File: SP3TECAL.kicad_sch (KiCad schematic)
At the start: 15 parts, among them IC1 MM5230-03NDB-TR, IC2 MM5230-03NDB-TR, IC3 MM5230-03NDB-TR, IC4 MM5230-03NDB-TR, J1 Conn_Coaxial, J2 Conn_Coaxial, J3 Conn_Coaxial, J4 Conn_Coaxial, J5 Conn_01x04, J6 Conn_01x04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

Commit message: much progress on routing
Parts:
- added R4, R5, R6: 56k, Resistor_SMD:R_0402_1005Metric, symbol Device:R
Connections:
- net GND: now also R4.1, R5.1, R6.1
- net at IC1.2 (RF2), IC3.4 (RF4): now also R5.2
- net at IC1.1 (RF1), IC4.3 (RF3): now also R4.2
- net at IC1.3 (RF3), IC2.1 (RF1): now also R6.2

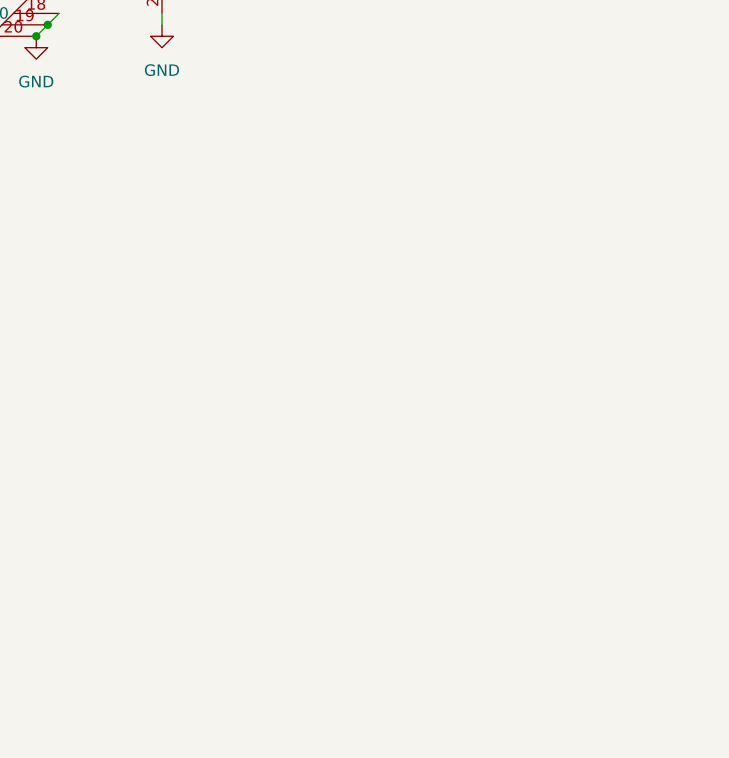
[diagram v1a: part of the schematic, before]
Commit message: used altium files to build kicad models of mm5800 and started new twpatron
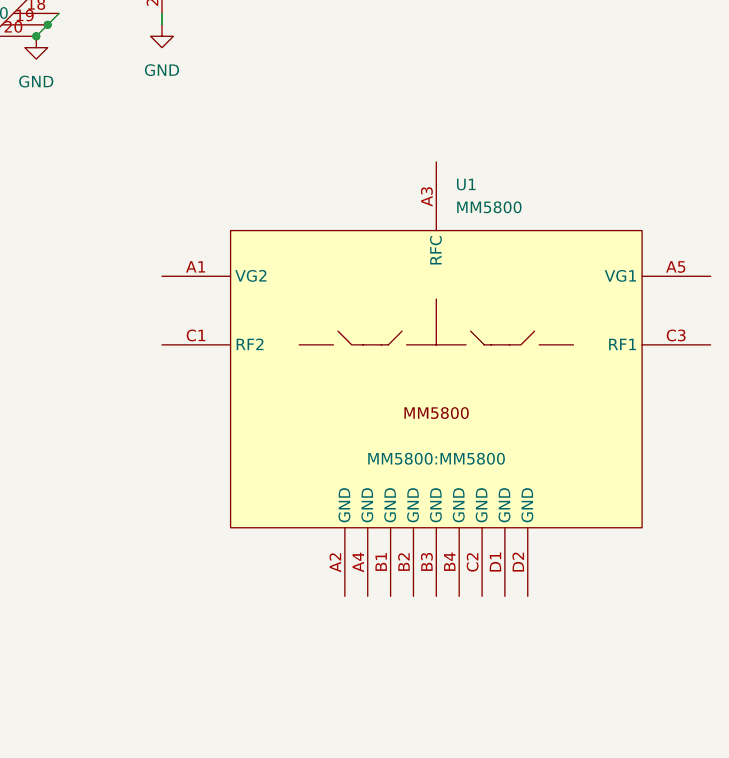
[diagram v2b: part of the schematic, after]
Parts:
- added U1: MM5800, MM5800:MM5800, symbol MM5800:MM5800.SCHLIB
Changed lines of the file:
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@@
+	)
+	(symbol
+		(lib_id "MM5800:MM5800.SCHLIB")
+		(at 245.11 123.19 0)
+		(unit 1)
+		(exclude_from_sim no)
+		(in_bom yes)
+		(on_board yes)
+		(dnp no)
+		(fields_autoplaced yes)
+		(property "Reference" "U1"
+			(at 247.2533 92.71 0)
+			(effects
+				(font
+					(size 1.27 1.27)
+				)
+				(justify left)
+			)
+		)
+		(property "Value" "MM5800"
+			(at 247.2533 95.25 0)
+			(effects
+				(font
+					(size 1.27 1.27)
+				)
+				(justify left)
+			)
+		)
+		(property "Footprint" "MM5800:MM5800"
+			(at 245.11 123.19 0)
+			(effects
+				(font
+					(size 1.27 1.27)
+				)
+			)
+		)
+		(property "Datasheet" ""
+			(at 245.11 123.19 0)
+			(effects
+				(font
+					(size 1.27 1.27)
+				)
+				(hide yes)
+			)
+		)
+		(property "Description" ""
+			(at 245.11 123.19 0)
+			(effects
+				(font
+					(size 1.27 1.27)
+				)
+				(hide yes)
+			)
+		)
+		(property "MANUFACTURER" "Menlo Micro"
+			(at 214.122 141.478 0)
+			(effects
+				(font
+					(size 1.27 1.27)
+				)
+				(justify left bottom)
+				(hide yes)
+			)
+		)
+		(property "MANUFACTURER_PART_NUMBER" "MM5800"
+			(at 214.122 141.478 0)
+			(effects
+				(font
+					(size 1.27 1.27)
+				)
+				(justify left bottom)
+				(hide yes)
+			)
+		)
+		(pin "A1"
+		)
+		(pin "C1"
+		)
+		(pin "B3"
+		)
+		(pin "A2"
+		)
+		(pin "B2"
+		)
+		(pin "D1"
+		)
+		(pin "B1"
+		)
+		(pin "A5"
+		)
+		(pin "A4"
+		)
+		(pin "C2"
+		)
+		(pin "A3"
+		)
+		(pin "C3"
+		)
+		(pin "B4"
+		)
+		(pin "D2"
+		)
+		(instances
+			(project ""
+				(path "/27633a03-897e-4d8a-8472-386b3ffbd891"
+					(reference "U1")
+					(unit 1)
+				)
+			)
+		)
 	)
 	(symbol
